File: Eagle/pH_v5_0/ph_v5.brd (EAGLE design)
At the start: 100 x 84.6 mm, 142 parts, among them CON1 JACK_DC_BARREL, IC1 MCP1703DB, IC2 TL084D, IC3 TL084D, IC5 TPS60400DBV, J1 RJ12RIGHTANGLE-I2C, J2 RJ12RIGHTANGLE-I2C, Q1 BSP75, Q2 BSP75, Q3 BSP75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

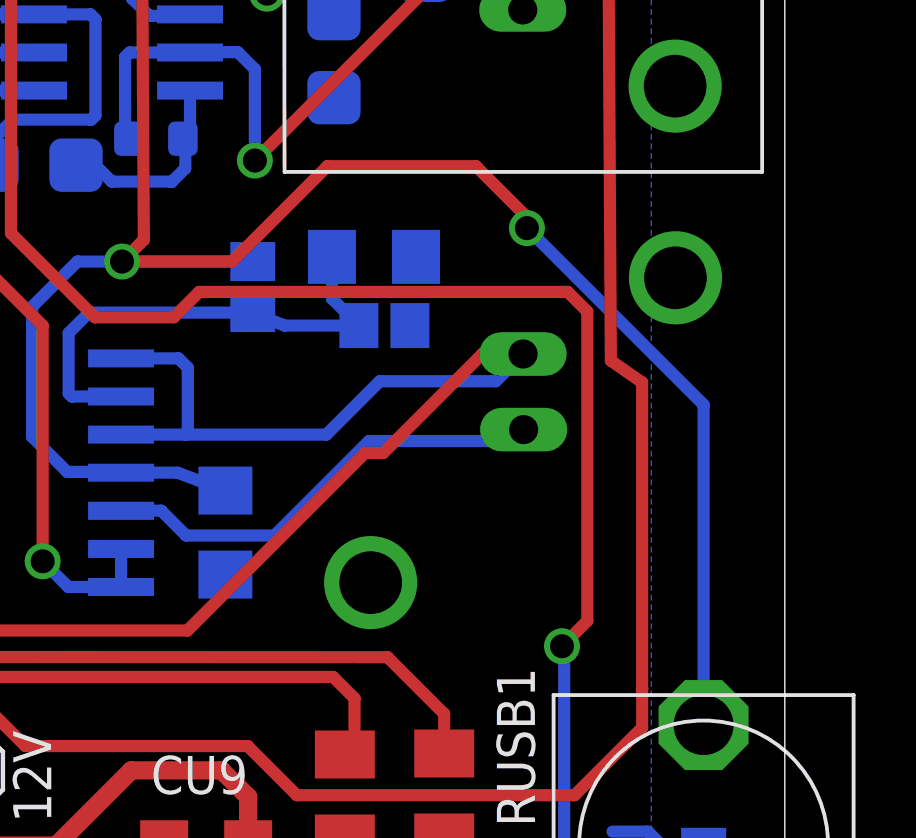
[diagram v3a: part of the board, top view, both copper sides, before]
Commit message: corected BCN connector side on phv5
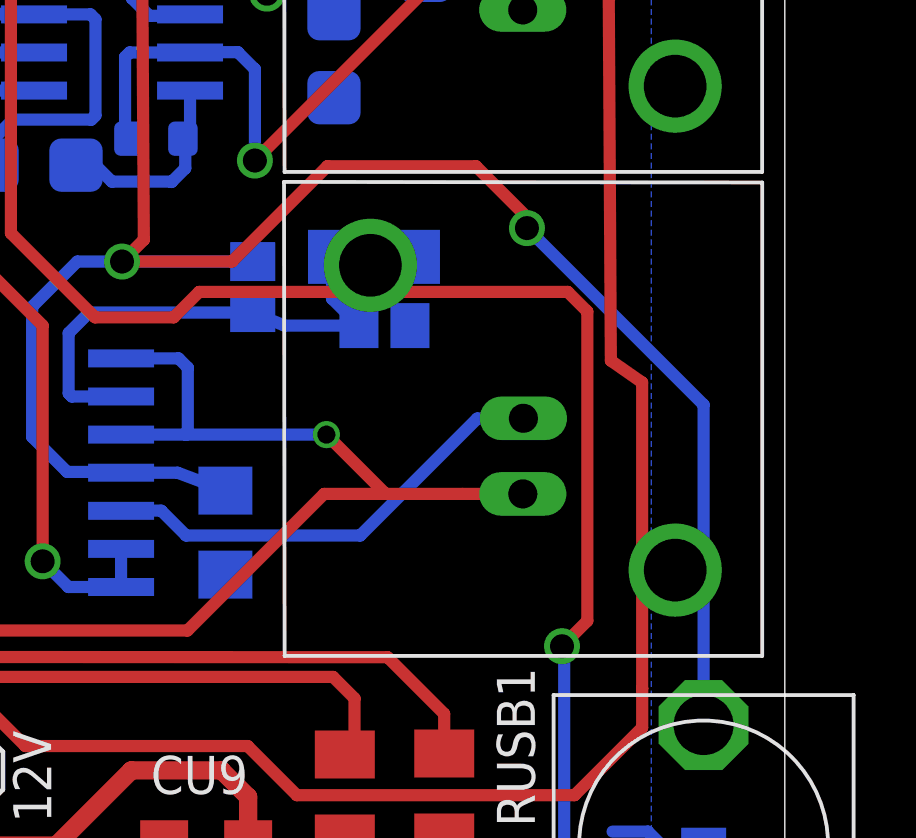
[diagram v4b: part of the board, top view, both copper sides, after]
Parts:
- moved U$2 15.5 mm to (78.3, 17.0), flipped to the top, turned to 90 degrees
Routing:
- net B-: track 106.1 -> 99.3 mm, vias 2 -> 3
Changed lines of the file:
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@@
 <?xml version="1.0" encoding="utf-8"?>
 <!DOCTYPE eagle SYSTEM "eagle.dtd">
-<eagle version="6.5.0">
+<eagle version="7.5.0">
 <drawing>
 <settings>
@@
 <pass name="Default">
 <param name="RoutingGrid" value="6mil"/>
+<param name="AutoGrid" value="1"/>
+<param name="Efforts" value="0"/>
+<param name="TopRouterVariant" value="1"/>
 <param name="tpViaShape" value="round"/>
 <param name="PrefDir.1" value="|"/>
@@
 <attribute name="VALUE" x="46.715725" y="33.91341875" size="1.27" layer="27" ratio="10" rot="R270"/>
 </element>
-<element name="U$2" library="phMeter" package="BNC-VERTICAL" value="BNC-VERTICAL" x="78.334784375" y="32.450834375" rot="MR270"/>
+<element name="U$2" library="phMeter" package="BNC-VERTICAL" value="BNC-VERTICAL" x="78.326190625" y="16.987478125" rot="R90"/>
 <element name="U$3" library="phMeter" package="VERTICAL-JACK" value="VERTICAL-JACK" x="87.2925875" y="15.681915625"/>
 <element name="C14" library="rcl" package="C1206" value="100n" x="76.351346875" y="21.0970875" smashed="yes" rot="MR270">
@@
 <wire x1="72.875353125" y1="24.3643" x2="75.038903125" y2="24.3643" width="0.4064" layer="16"/>
 <wire x1="75.038903125" y1="24.3643" x2="79.719040625" y2="24.3643" width="0.4064" layer="16"/>
-<wire x1="79.719040625" y1="24.3643" x2="81.496153125" y2="26.1414125" width="0.4064" layer="16"/>
-<wire x1="81.496153125" y1="26.1414125" x2="85.3653625" y2="26.1414125" width="0.4064" layer="16"/>
-<wire x1="85.3653625" y1="26.1414125" x2="86.274784375" y2="27.050834375" width="0.4064" layer="16"/>
 <wire x1="65.148196875" y1="29.49846875" x2="65.148196875" y2="18.345290625" width="0.4064" layer="1"/>
 <wire x1="65.148196875" y1="18.345290625" x2="65.65983125" y2="17.83365625" width="0.4064" layer="1"/>
 <wire x1="65.65983125" y1="17.83365625" x2="75.088690625" y2="17.83365625" width="0.4064" layer="1"/>
-<wire x1="75.088690625" y1="17.83365625" x2="81.00888125" y2="23.753846875" width="0.4064" layer="1"/>
-<wire x1="81.00888125" y1="23.753846875" x2="81.6180625" y2="23.753846875" width="0.4064" layer="1"/>
-<wire x1="81.6180625" y1="23.753846875" x2="84.93141875" y2="27.067203125" width="0.4064" layer="1"/>
-<wire x1="84.93141875" y1="27.067203125" x2="86.258415625" y2="27.067203125" width="0.4064" layer="1"/>
-<wire x1="86.258415625" y1="27.067203125" x2="86.274784375" y2="27.050834375" width="0.4064" layer="1"/>
 <wire x1="72.875353125" y1="26.9043" x2="74.7917" y2="26.9043" width="0.4064" layer="16"/>
 <wire x1="74.7917" y1="26.9043" x2="75.0998125" y2="26.5961875" width="0.4064" layer="16"/>
@@
 <wire x1="65.62645625" y1="29.976728125" x2="65.62645625" y2="30.724109375" width="0.4064" layer="16"/>
 <wire x1="65.62645625" y1="30.724109375" x2="63.2042125" y2="33.146353125" width="0.4064" layer="16"/>
+<wire x1="75.088690625" y1="17.83365625" x2="79.6425125" y2="22.387478125" width="0.4064" layer="1"/>
+<wire x1="79.6425125" y1="22.387478125" x2="81.6958625" y2="22.387478125" width="0.4064" layer="1"/>
+<via x="79.719040625" y="24.3643" extent="1-16" drill="0.6" shape="square"/>
+<wire x1="84.257196875" y1="22.387478125" x2="86.266190625" y2="22.387478125" width="0.4064" layer="1"/>
+<wire x1="79.719040625" y1="24.3643" x2="81.6958625" y2="22.387478125" width="0.4064" layer="1"/>
+<wire x1="81.6958625" y1="22.387478125" x2="84.257196875" y2="22.387478125" width="0.4064" layer="1"/>
 </signal>
 <signal name="N$1">
@@
 <contactref element="U$2" pad="S"/>
 <contactref element="IC2" pad="5"/>
-<wire x1="85.913615625" y1="24.149665625" x2="86.294784375" y2="24.530834375" width="0.4064" layer="16"/>
-<wire x1="85.913615625" y1="24.149665625" x2="81.139575" y2="24.149665625" width="0.4064" layer="16"/>
-<wire x1="81.139575" y1="24.149665625" x2="77.990746875" y2="21.0008375" width="0.4064" layer="16"/>
-<wire x1="77.990746875" y1="21.0008375" x2="75.0425875" y2="21.0008375" width="0.4064" layer="16"/>
+<wire x1="80.84716875" y1="21.0008375" x2="75.0425875" y2="21.0008375" width="0.4064" layer="16"/>
 <wire x1="75.0425875" y1="21.0008375" x2="74.21425" y2="21.829175" width="0.4064" layer="16"/>
 <wire x1="74.21425" y1="21.829175" x2="72.880228125" y2="21.829175" width="0.4064" layer="16"/>
 <wire x1="72.880228125" y1="21.829175" x2="72.875353125" y2="21.8243" width="0.4064" layer="16"/>
+<wire x1="80.84716875" y1="21.0008375" x2="84.745340625" y2="24.899009375" width="0.4064" layer="16"/>
+<wire x1="84.745340625" y1="24.899009375" x2="86.277721875" y2="24.899009375" width="0.4064" layer="16"/>
+<wire x1="86.277721875" y1="24.899009375" x2="86.286190625" y2="24.907478125" width="0.4064" layer="16"/>
 </signal>
 <signal name="N$27">

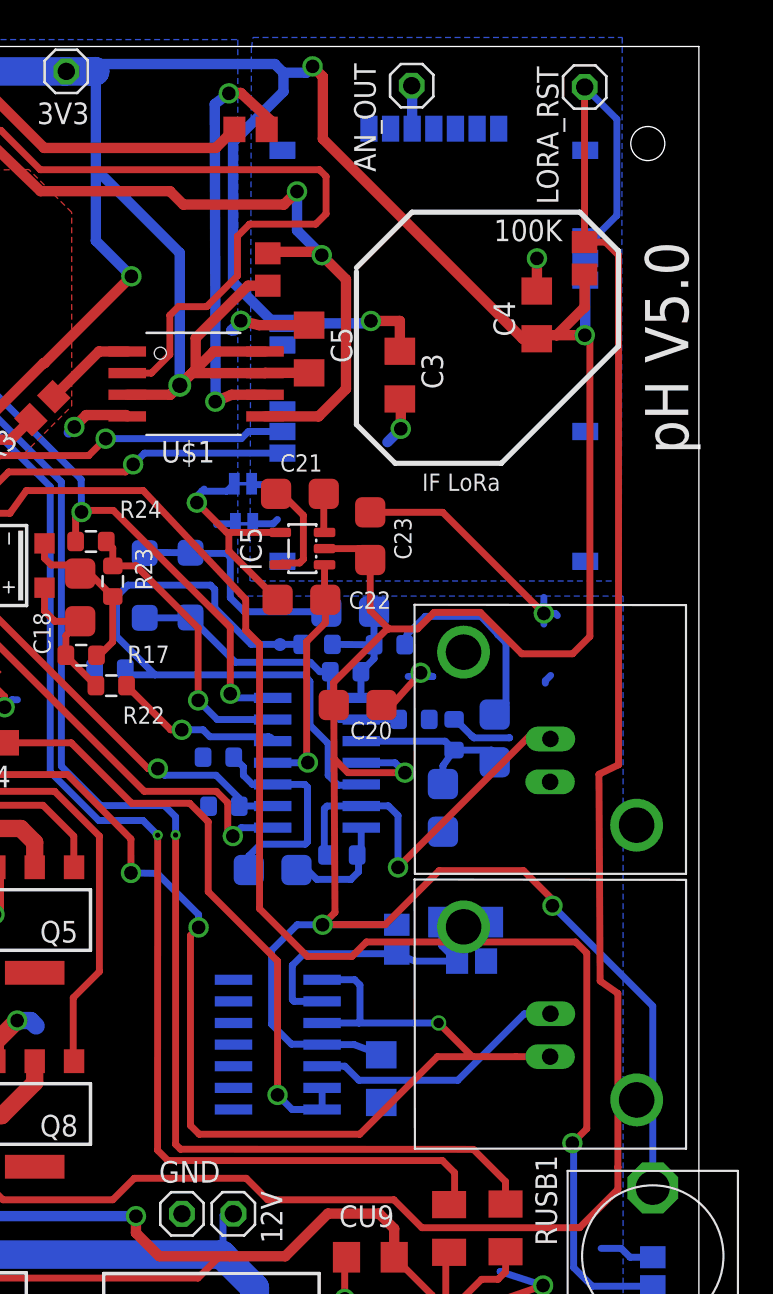
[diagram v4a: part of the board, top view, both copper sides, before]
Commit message: Added SMA LoRa antenna for phV5 board extra mistakes fixed with DRC close #18
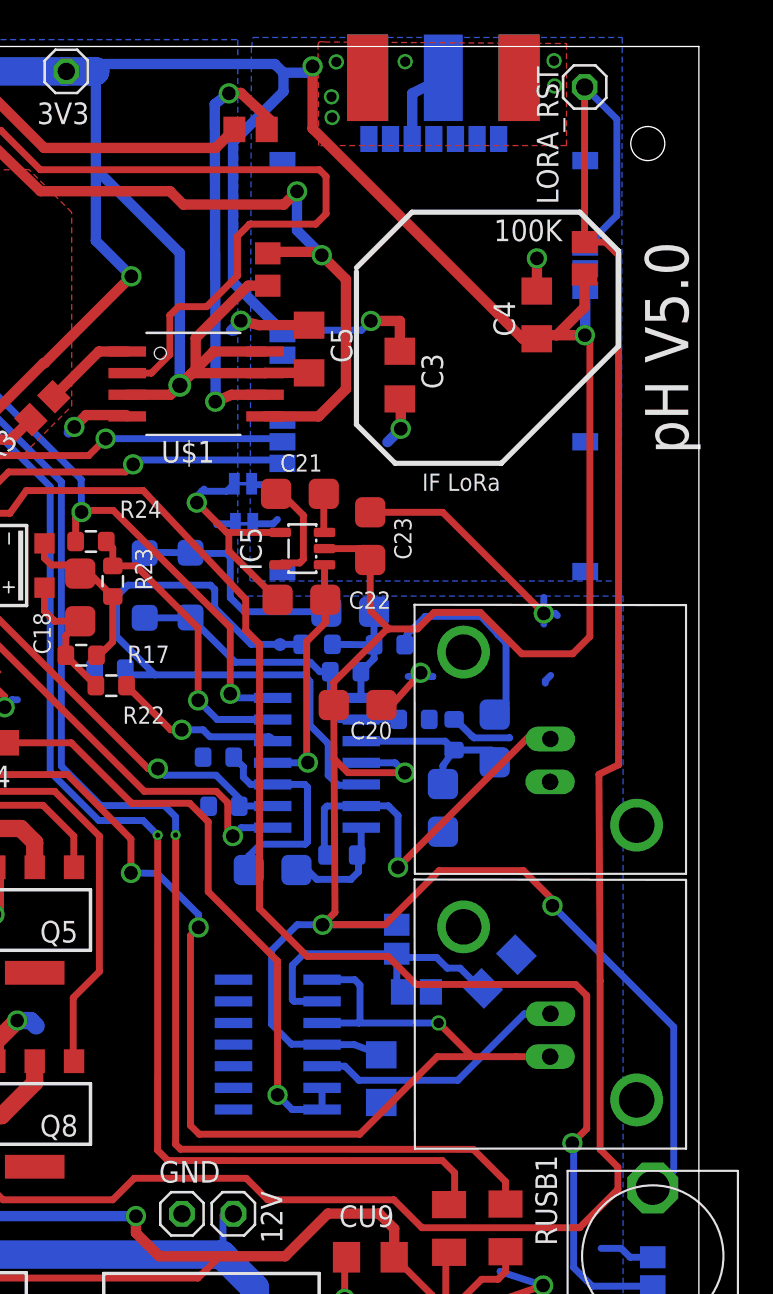
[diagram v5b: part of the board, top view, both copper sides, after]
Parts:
- removed AN_OUT: (no value), Headerlibrary:1X01
- added 868MHZ: (no value), sma_end_launch:SMA_EDGELAUNCH
- moved R8 3.71 mm to (78.4, 26.2)
- moved C15 3.52 mm to (83.3, 27.4), turned to 315 degrees
- moved U100 0.60 mm to (88.3, 49.6)
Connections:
- net ANGND: now also 868MHZ.GND@1, 868MHZ.GND@2, 868MHZ.GND@3, 868MHZ.GND@4
- net ANT868: now also 868MHZ.P; no longer AN_OUT.1
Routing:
- net N$27: track 16.5 -> 19.4 mm
- net ANT868: track 2.54 -> 4.72 mm
- net A4: track 115.0 -> 112.8 mm
- net 3.3V: track 535.0 -> 536.0 mm
- net ANGND: vias 2 -> 8
- added copper zone on layer 1, net ANGND
